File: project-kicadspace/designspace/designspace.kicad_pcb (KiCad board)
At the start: 2 copper layers, 68.5 x 51 mm, 35 parts, among them J1 PJ-342S

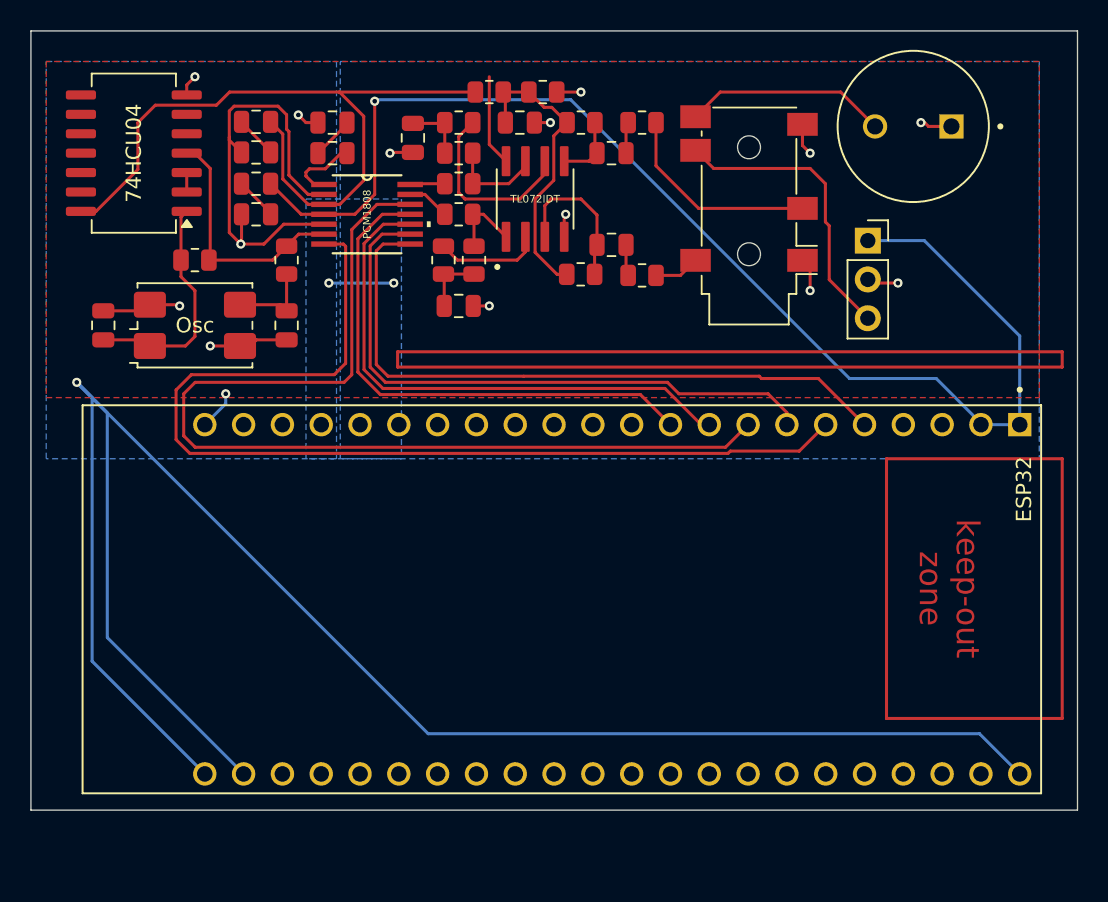
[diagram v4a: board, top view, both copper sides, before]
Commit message: feat(pcb): increase track size for power line & redirect 5V power line to 74HCU04 & PCM1808
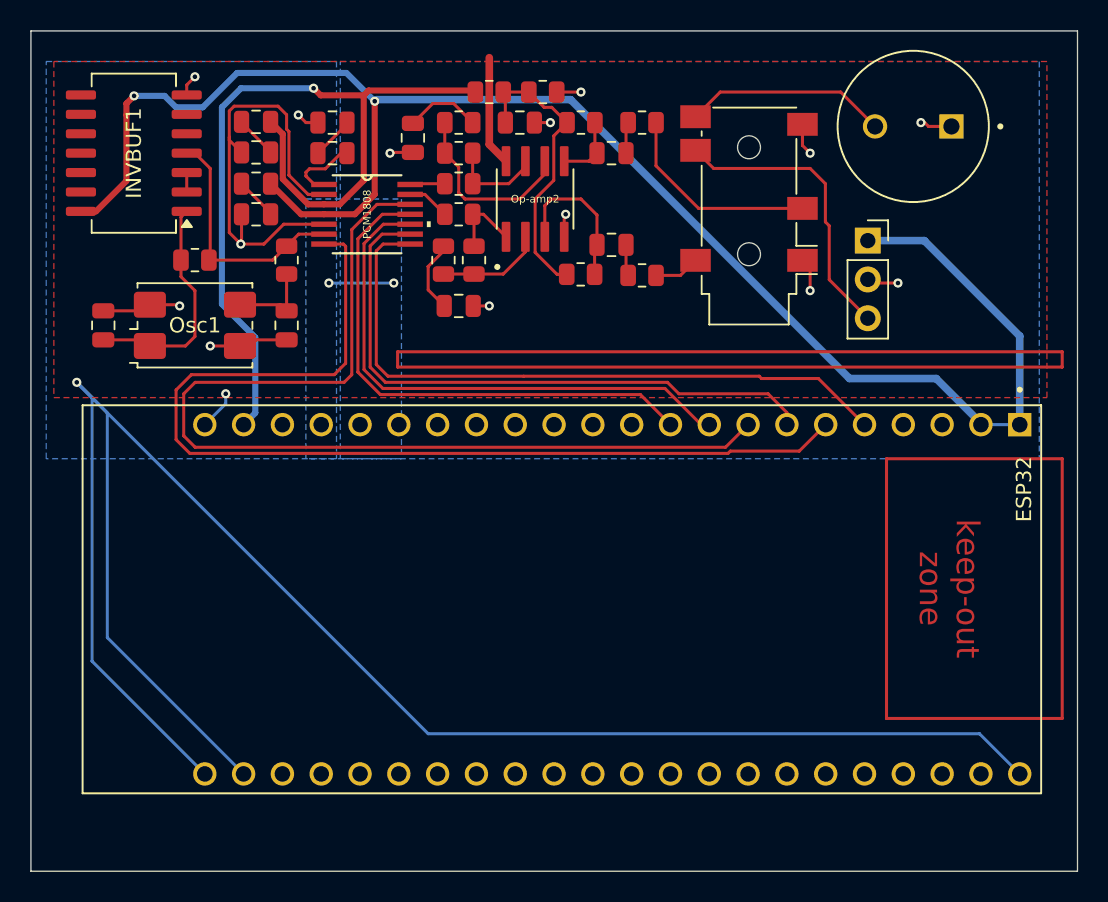
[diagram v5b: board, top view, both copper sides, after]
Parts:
- J1: value PJ-342S -> PJ-313B
- renumbered 74HCU04 to INVBUF1, TL072IDT to Op-amp2, Osc to Osc1
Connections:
- ESP32 pad 5V0: unconnected-(ESP32-Pad5V0) -> 5V
- INVBUF1 pad 14: 5V -> 3.3V
- R13 pad 2: Net-(C14-Pad2) -> Net-(Op-amp2B--)
- R14 pad 1: Net-(Op-amp2B--) -> Net-(C14-Pad2)
- R14 pad 2: Net-(C14-Pad2) -> Net-(Op-amp2B--)
- R4 pad 2: Net-(C10-Pad2) -> Net-(Op-amp2A--)
- R5 pad 1: Net-(Op-amp2A--) -> Net-(C10-Pad2)
- R5 pad 2: Net-(C10-Pad2) -> Net-(Op-amp2A--)
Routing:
- net 3.3V: track 83.7 -> 111.1 mm, vias 1 -> 2
- net 5V: track 48.0 -> 55.7 mm, vias 0 -> 1
- net 9V: track 5.98 -> 7.23 mm
- net Net-(C14-Pad2): track 4.11 -> 4.97 mm
- net Net-(C10-Pad2): track 4.11 -> 4.95 mm
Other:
- board size 68.5 x 51 mm -> 68.5 x 55 mm

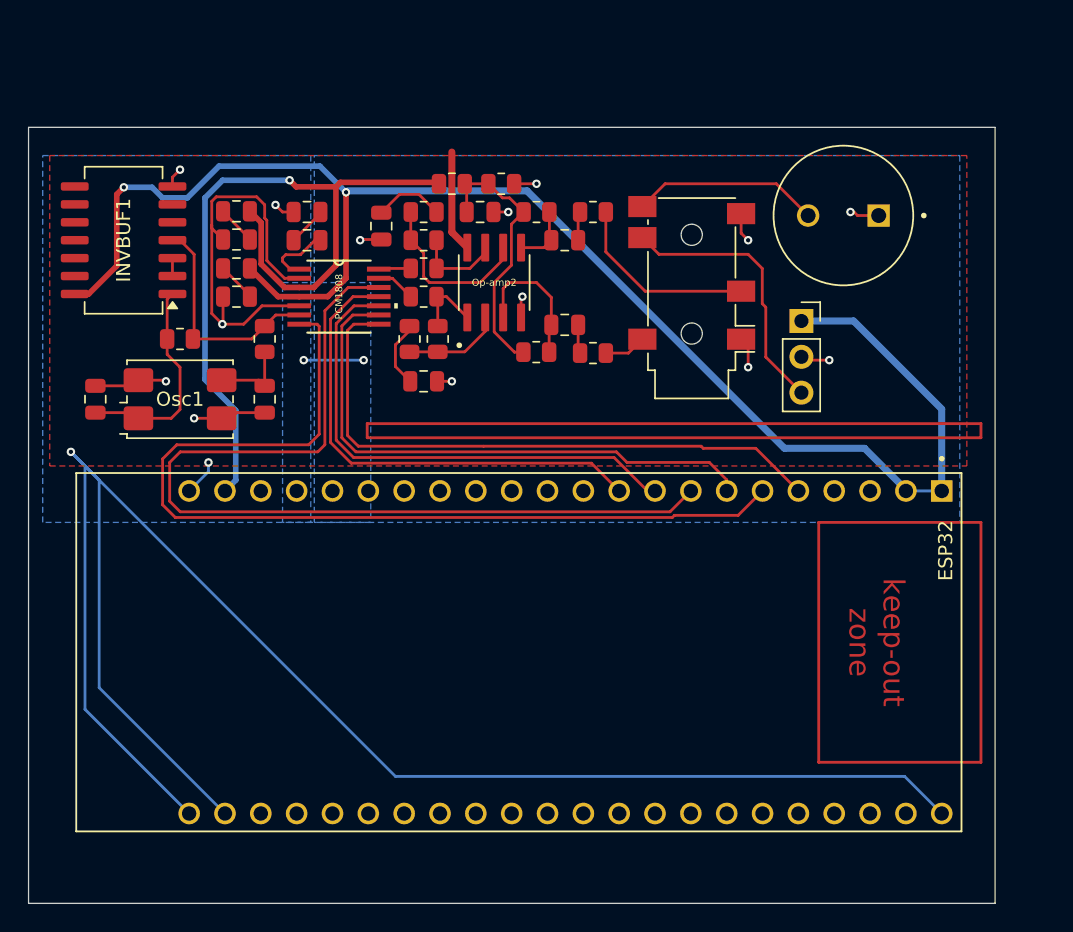
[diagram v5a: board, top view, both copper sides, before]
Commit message: feat(pcb): import pin socket for voltage divider source 12->12/5/3.3, prepared for final validation to pcb manufacturing
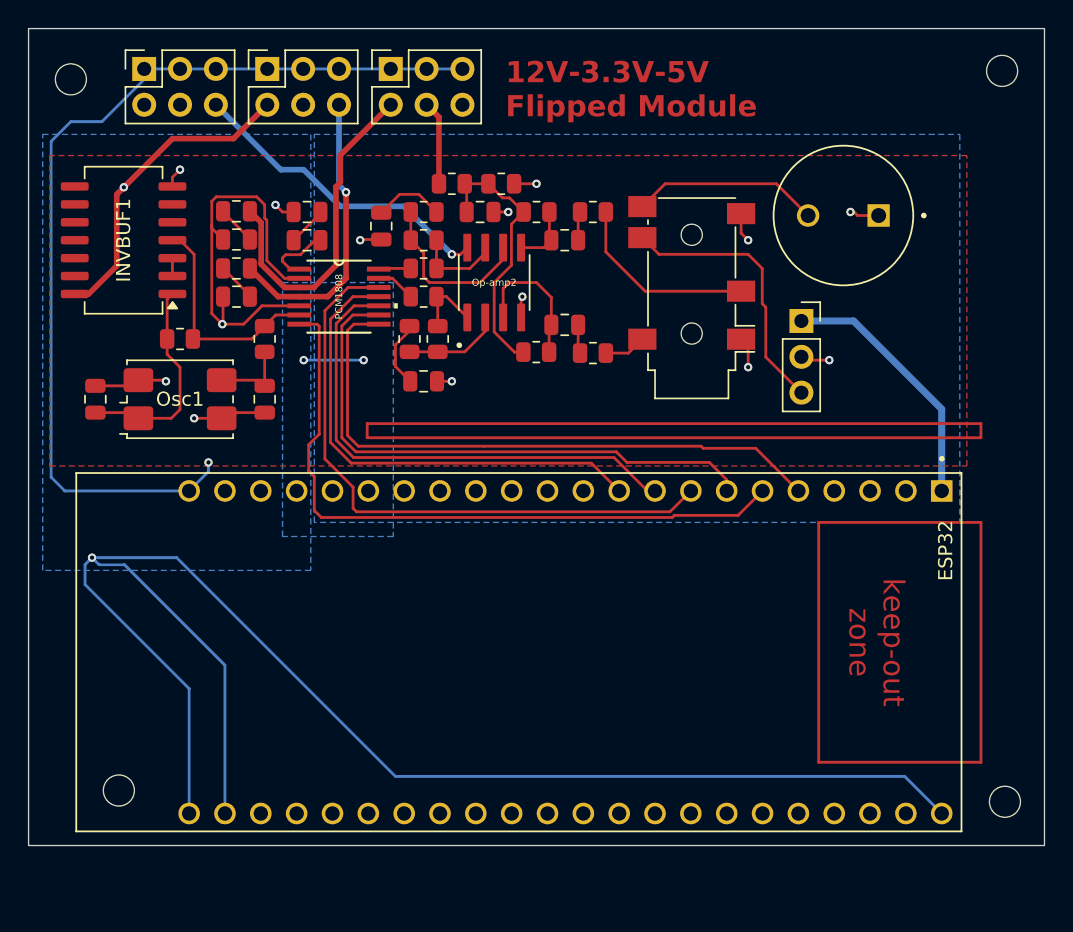
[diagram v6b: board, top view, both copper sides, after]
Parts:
- added REF**: MountingHole_2.2mm_M2, MountingHole:MountingHole_2.2mm_M2, F.Cu at (47.0, 61.6)
- added REF**: PinSocket_2x03_P2.54mm_Vertical, Connector_PinSocket_2.54mm:PinSocket_2x03_P2.54mm_Vertical, F.Cu at (52.2, 60.9)
- added REF**: PinSocket_2x03_P2.54mm_Vertical, Connector_PinSocket_2.54mm:PinSocket_2x03_P2.54mm_Vertical, F.Cu at (69.7, 60.9)
- added REF**: MountingHole_2.2mm_M2, MountingHole:MountingHole_2.2mm_M2, F.Cu at (113.0, 61.0)
- added REF**: MountingHole_2.2mm_M2, MountingHole:MountingHole_2.2mm_M2, F.Cu at (113.2, 112.8)
- added REF**: MountingHole_2.2mm_M2, MountingHole:MountingHole_2.2mm_M2, F.Cu at (50.4, 112.0)
- added REF**: PinSocket_2x03_P2.54mm_Vertical, Connector_PinSocket_2.54mm:PinSocket_2x03_P2.54mm_Vertical, F.Cu at (60.9, 60.9)
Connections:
- ESP32 pad 3V3.: 3.3V -> unconnected-(ESP32-Pad3V3.)
- ESP32 pad 5V0: 5V -> unconnected-(ESP32-Pad5V0)
- Op-amp2 pad 8: 9V -> 12V
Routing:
- net 3.3V: track 111.1 -> 61.3 mm
- net GND: track 196.1 -> 243.4 mm
- net 5V: track 55.7 -> 29.8 mm, vias 1 -> 0
- net 12V: track 0.00 -> 22.4 mm, vias 0 -> 1
- net Net-(PCM1808-FMT): track 66.1 -> 44.0 mm
- net Net-(PCM1808-LRCK): track 67.9 -> 47.8 mm
- net 9V: track 7.23 -> 0.00 mm
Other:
- board size 68.5 x 55 mm -> 72 x 57.9 mm
- board text added: "12V-3.3V-5V Flipped Module"

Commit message: feat(gerber): export gerber filer to prepare for pcb manufacturing
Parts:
- moved REF** 5.97 mm to (44.6, 113.4)
- moved REF** 2.60 mm to (44.6, 60.6)
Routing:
- net GND: track 243.4 -> 198.1 mm, vias 18 -> 19
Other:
- board size 72 x 57.9 mm -> 74 x 58 mm

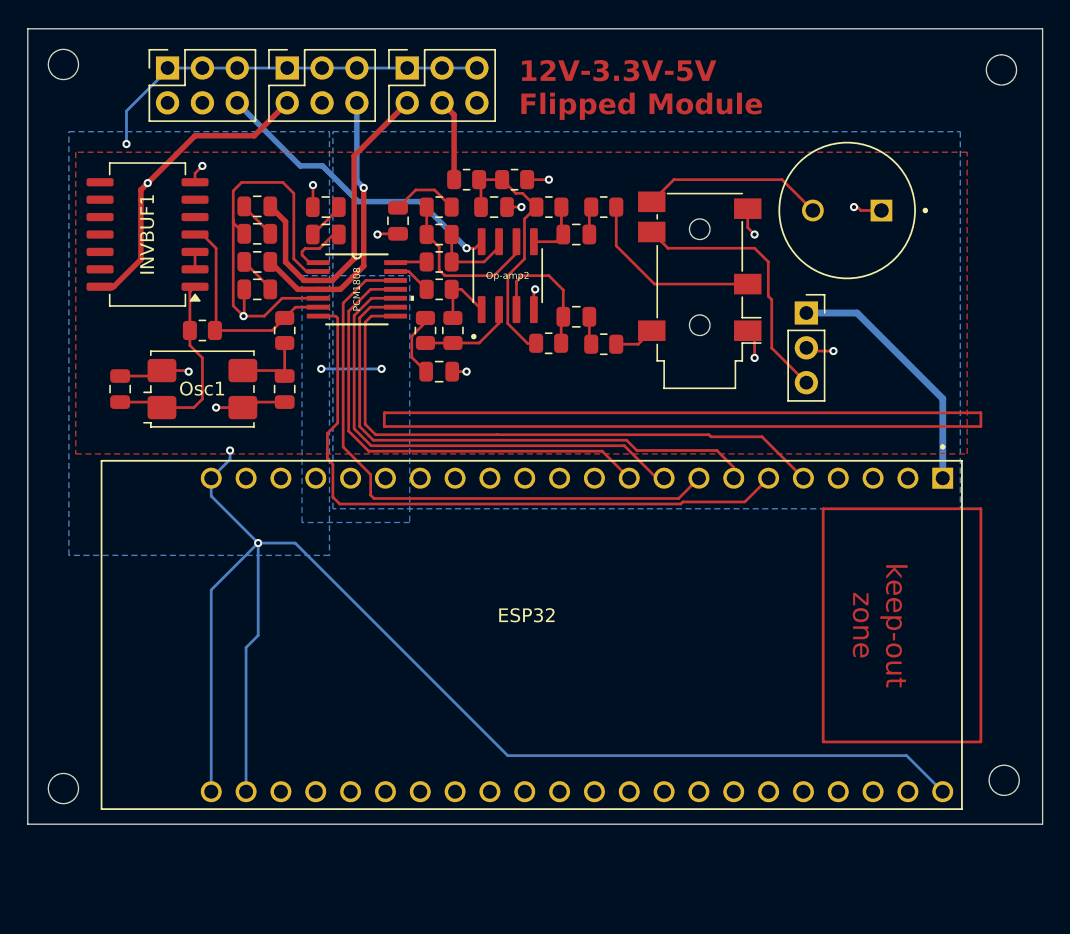
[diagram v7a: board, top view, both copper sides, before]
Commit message: feat(pcb): add round corner & adjust size for actual components
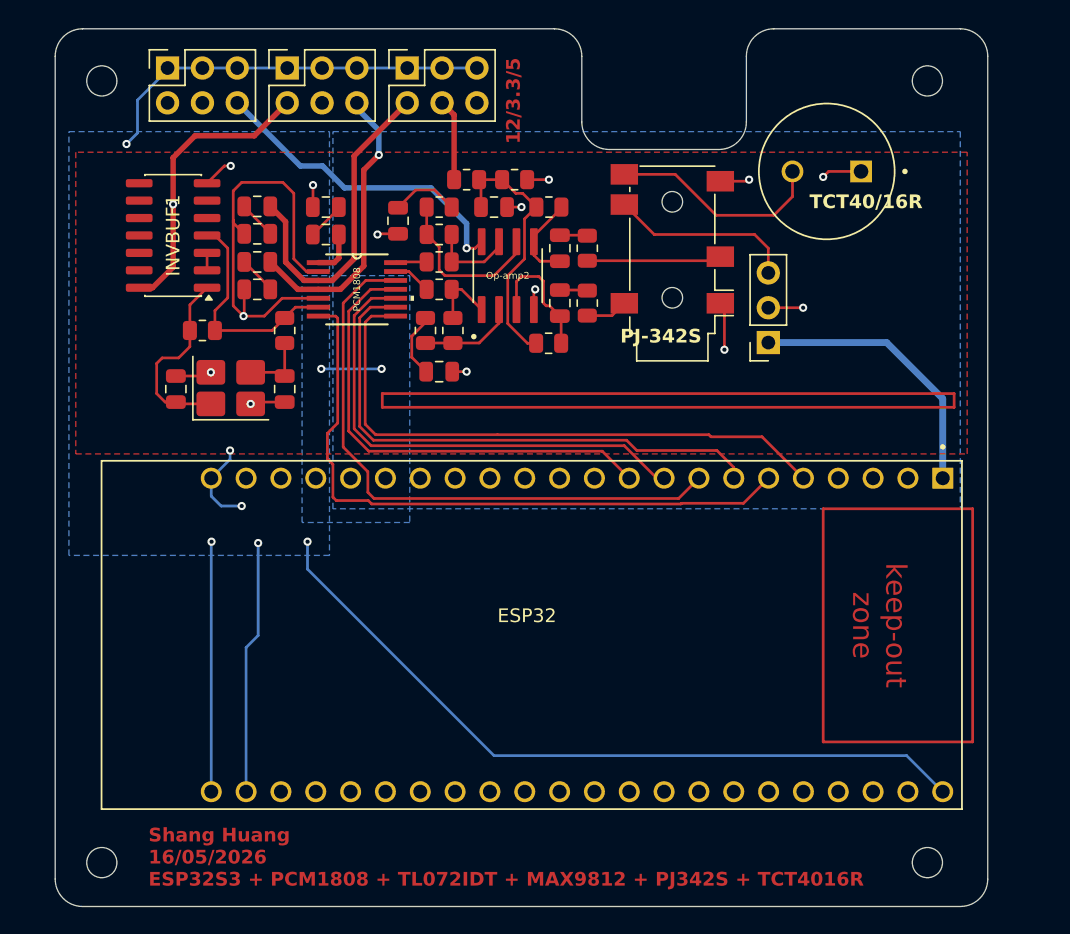
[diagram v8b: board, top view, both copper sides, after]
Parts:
- INVBUF1: footprint Package_SO:SO-14_5.3x10.2mm_P1.27mm -> Package_SO:SO-14_3.9x8.65mm_P1.27mm
- Osc1: footprint Crystal:Crystal_SMD_7050-4Pin_7.0x5.0mm -> Crystal:Crystal_SMD_3225-4Pin_3.2x2.5mm_HandSoldering
- moved REF** 8.21 mm to (107.6, 118.8)
- moved REF** 6.08 mm to (47.4, 118.8)
- moved REF** 5.46 mm to (107.6, 61.8)
- moved C11 4.07 mm to (52.8, 84.3)
- moved REF** 3.51 mm to (96.0, 80.9), turned to 180 degrees
- moved R10 3.23 mm to (82.8, 78.0), turned to -90 degrees
- moved R11 3.23 mm to (82.8, 74.0), turned to -90 degrees
- moved MK2 3.21 mm to (100.3, 68.4)
- moved REF** 3.05 mm to (47.4, 61.8)
- moved J1 2.83 mm to (89.0, 73.3)
- moved Osc1 2.07 mm to (56.8, 84.2)
- moved INVBUF1 1.87 mm to (52.6, 73.1)
- moved C15 1.56 mm to (80.8, 74.0), turned to 90 degrees
- moved C3 1.56 mm to (80.8, 78.0), turned to 90 degrees
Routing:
- net GND: track 198.1 -> 190.4 mm, vias 19 -> 22
- net Net-(U3-OUT): track 19.4 -> 13.6 mm
- net Net-(J1-PadR1): track 13.6 -> 9.82 mm
- net Net-(MK2-+): track 13.4 -> 15.9 mm
- net Net-(Op-amp2B-+): track 4.48 -> 6.93 mm
- net 3.3V: track 61.1 -> 62.6 mm
- net Net-(PCM1808-VREF): track 4.86 -> 3.75 mm
- net 12V: track 22.4 -> 23.5 mm
- net Net-(C11-Pad1): track 15.1 -> 14.2 mm
- net Net-(Op-amp2A-+): track 10.0 -> 9.52 mm
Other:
- board size 74 x 58 mm -> 68 x 64 mm
- board text added: "12/3.3/5"
- board text added: "PJ-342S"
- board text added: "Shang Huang 16/05/2026 ESP32S3 + PCM1808 + TL072IDT + MAX9812 + PJ342S + TCT4016R"
- board text added: "TCT40/16R"
- board text removed: "12V-3.3V-5V Flipped Module"
